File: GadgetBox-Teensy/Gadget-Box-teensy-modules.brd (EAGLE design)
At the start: 93.5 x 53.5 mm, 15 parts, among them U3 TEENSY_3.1_ALL_PINS

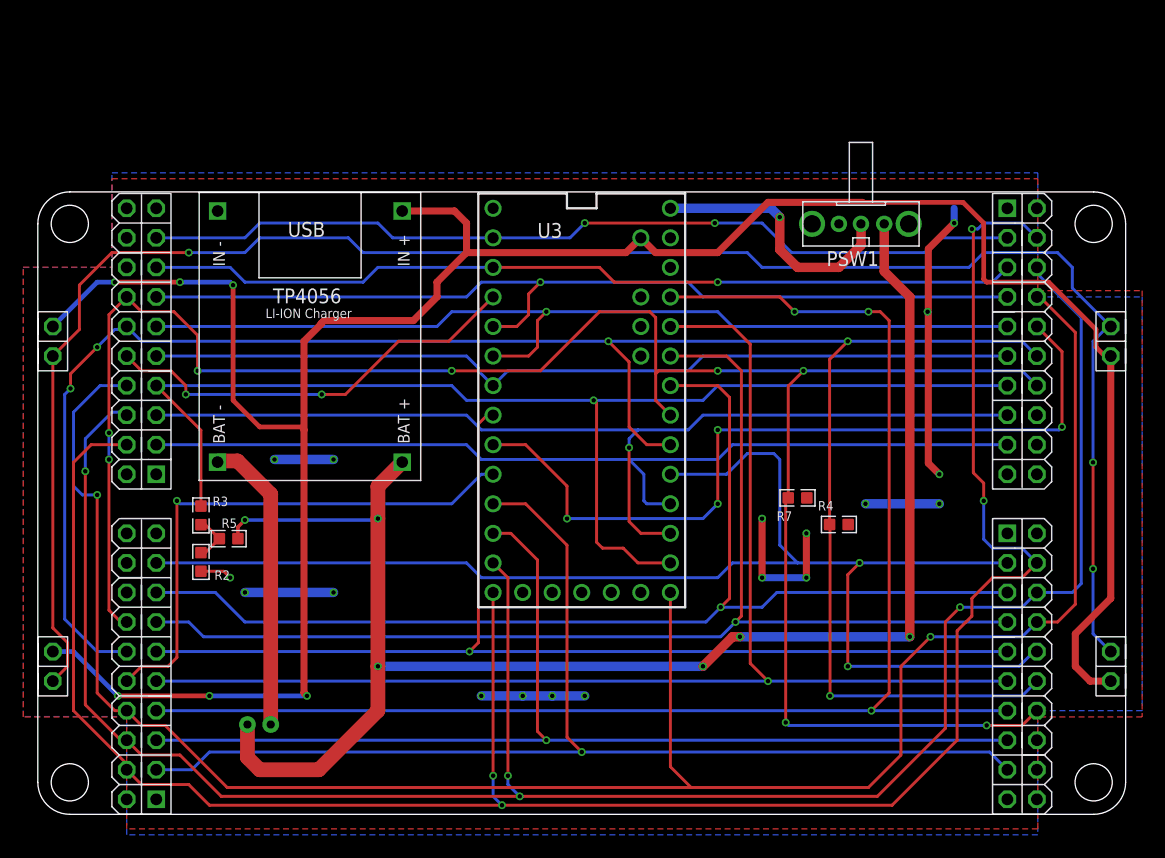
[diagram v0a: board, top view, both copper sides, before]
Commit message: Fixed charging circuit
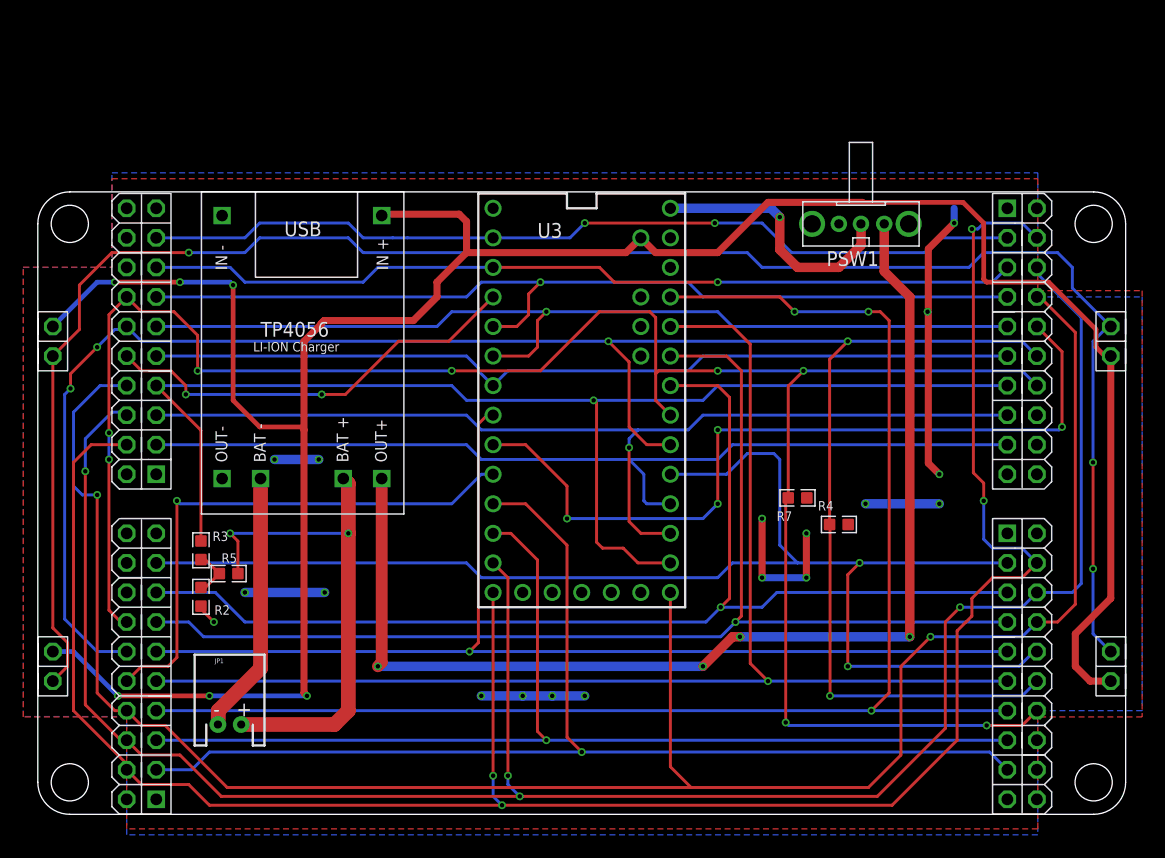
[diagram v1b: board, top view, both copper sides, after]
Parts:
- moved R2 3.00 mm to (15.3, 19.9)
- moved R3 3.00 mm to (15.3, 23.9)
- moved R5 3.00 mm to (17.7, 21.9)
- moved U$1 3.00 mm to (24.0, 39.0)
- moved JP1 2.54 mm to (17.7, 8.97), flipped to the top
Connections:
- removed net VBATTERY: JP1.2, PSW1.1, R5.2, U$1.BAT+
- new net VBATTTERY: JP1.2, R5.2, U$1.BAT+
- new net VOUT: PSW1.1, U$1.OUT+
- net GND: now also U$1.OUT-
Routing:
- net VBATTERY: track 135.3 -> 0.00 mm, vias 6 -> 0
- net VOUT: track 0.00 -> 99.4 mm, vias 0 -> 4
- net VBATTTERY: track 0.00 -> 43.7 mm, vias 0 -> 2
- net GND: track 65.2 -> 61.5 mm
- net D5/A0: track 105.5 -> 108.5 mm
- net 3V3: track 27.9 -> 25.9 mm
- net VUSB: track 213.6 -> 215.3 mm
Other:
- board text removed: "BAT"

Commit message: Fixed Silkscreen
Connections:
- removed net RESET: AH.RESET@2, AL.RESET@2, BH.RESET@2, BL.RESET@2
- net VUSB: now also AH.5V@B7, AL.5V@B7, BH.5V@B7, BL.5V@B7; no longer AH.5V@2, AL.5V@2, BH.5V@2, BL.5V@2
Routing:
- net RESET: track 161.0 -> 0.00 mm, vias 3 -> 0
- net VUSB: track 215.3 -> 203.2 mm, vias 6 -> 5
- net GND: track 61.5 -> 67.6 mm, vias 8 -> 10
- net SPI-MOSI: track 179.0 -> 180.9 mm
- net I2C-SDA: track 175.3 -> 176.4 mm

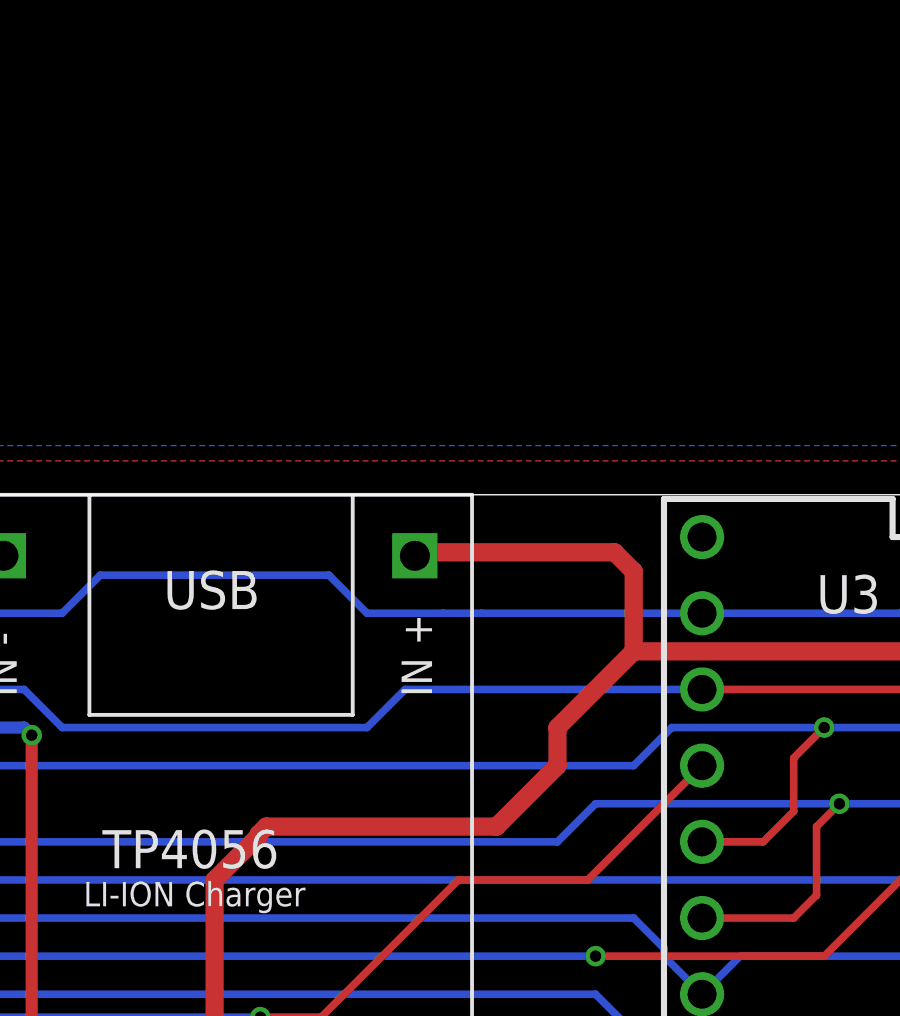
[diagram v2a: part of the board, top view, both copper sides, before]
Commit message: Added battery cable cutout
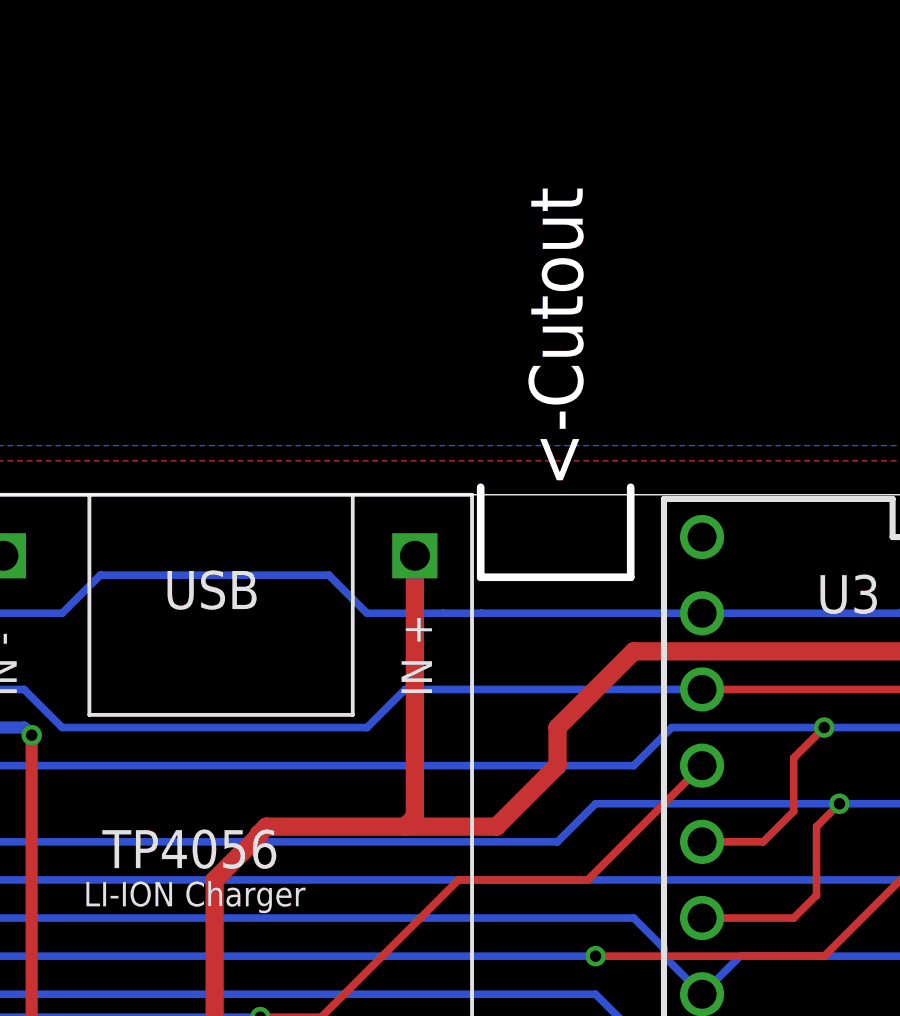
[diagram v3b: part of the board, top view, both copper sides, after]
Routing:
- net VUSB: track 203.2 -> 202.1 mm
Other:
- board text added: "<-Cutout"
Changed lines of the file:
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@@
 <wire x1="49.007" y1="26.416" x2="89.9006" y2="26.416" width="0.254" layer="200"/>
 <wire x1="49.007" y1="26.67" x2="89.1722" y2="26.67" width="0.254" layer="200"/>
+<wire x1="33" y1="55" x2="33" y2="52" width="0.254" layer="20"/>
+<wire x1="33" y1="52" x2="38" y2="52" width="0.254" layer="20"/>
+<wire x1="38" y1="52" x2="38" y2="55" width="0.254" layer="20"/>
+<text x="36.4" y="55" size="1.778" layer="20" font="vector" ratio="15" rot="R90">&lt;-Cutout</text>
 </plain>
 <attributes>
@@
 <wire x1="13.462" y1="46.99" x2="17.78" y2="46.99" width="0.4064" layer="16"/>
 <wire x1="17.78" y1="46.99" x2="18.034" y2="46.736" width="0.4064" layer="16"/>
-<wire x1="25.854" y1="43.688" x2="33.528" y2="43.688" width="0.6096" layer="1"/>
+<wire x1="25.854" y1="43.688" x2="30.48" y2="43.688" width="0.6096" layer="1"/>
+<wire x1="30.48" y1="43.688" x2="33.528" y2="43.688" width="0.6096" layer="1"/>
 <wire x1="33.528" y1="43.688" x2="35.56" y2="45.72" width="0.6096" layer="1"/>
 <wire x1="35.56" y1="45.72" x2="35.56" y2="46.99" width="0.6096" layer="1"/>
@@
 <wire x1="54.35" y1="49.53" x2="53.08" y2="50.8" width="0.6096" layer="1"/>
 <contactref element="U$1" pad="IN+"/>
-<wire x1="38.1" y1="52.197" x2="38.1" y2="49.53" width="0.6096" layer="1"/>
 <wire x1="25.6" y1="43.434" x2="25.6" y2="43.38" width="0.6096" layer="1"/>
 <wire x1="25.6" y1="43.38" x2="24.13" y2="41.91" width="0.6096" layer="1"/>
@@
 <wire x1="20.32" y1="34.544" x2="23.876" y2="34.544" width="0.4064" layer="1"/>
 <wire x1="23.876" y1="34.544" x2="24.13" y2="34.29" width="0.4064" layer="1"/>
-<wire x1="38.1" y1="52.197" x2="37.465" y2="52.832" width="0.6096" layer="1"/>
-<wire x1="37.465" y1="52.832" x2="30.9232" y2="52.832" width="0.6096" layer="1"/>
-<wire x1="30.9232" y1="52.832" x2="30.8072" y2="52.716" width="0.6096" layer="1"/>
 <contactref element="BH" pad="5V@B7"/>
 <contactref element="AL" pad="5V@B7"/>
@@
 <wire x1="88.9" y1="7.62" x2="88.9" y2="6.858" width="0.4064" layer="1"/>
 <wire x1="88.9" y1="6.858" x2="87.122" y2="5.08" width="0.4064" layer="1"/>
+<wire x1="30.8072" y1="52.716" x2="30.8072" y2="44.0152" width="0.6096" layer="1"/>
+<wire x1="30.8072" y1="44.0152" x2="30.48" y2="43.688" width="0.6096" layer="1"/>
 </signal>
 <signal name="N$2">
